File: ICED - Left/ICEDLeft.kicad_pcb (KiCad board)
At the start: 2 copper layers, 175.4 x 145 mm, 164 parts, among them P1 Conn_ARM_JTAG_SWD_10, P2 DX07S024XJ1R1100, P3 CONN_17, P4 692121130100, P5 RGB Out, Q1 TC1264, U1 MK20DX256VLH7, U2 IS31FL3737-QFLS4-TR, X1 CRYSTAL

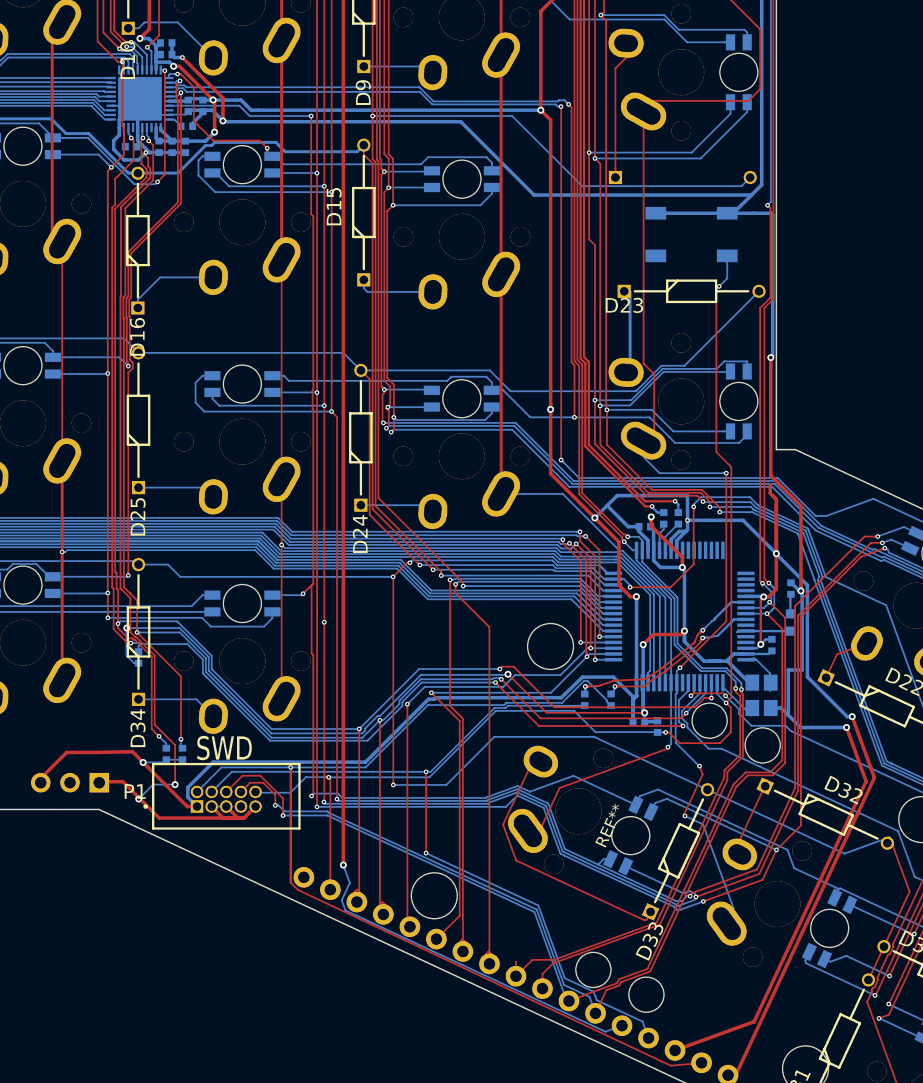
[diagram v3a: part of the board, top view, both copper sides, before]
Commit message: re-added RGBOUT
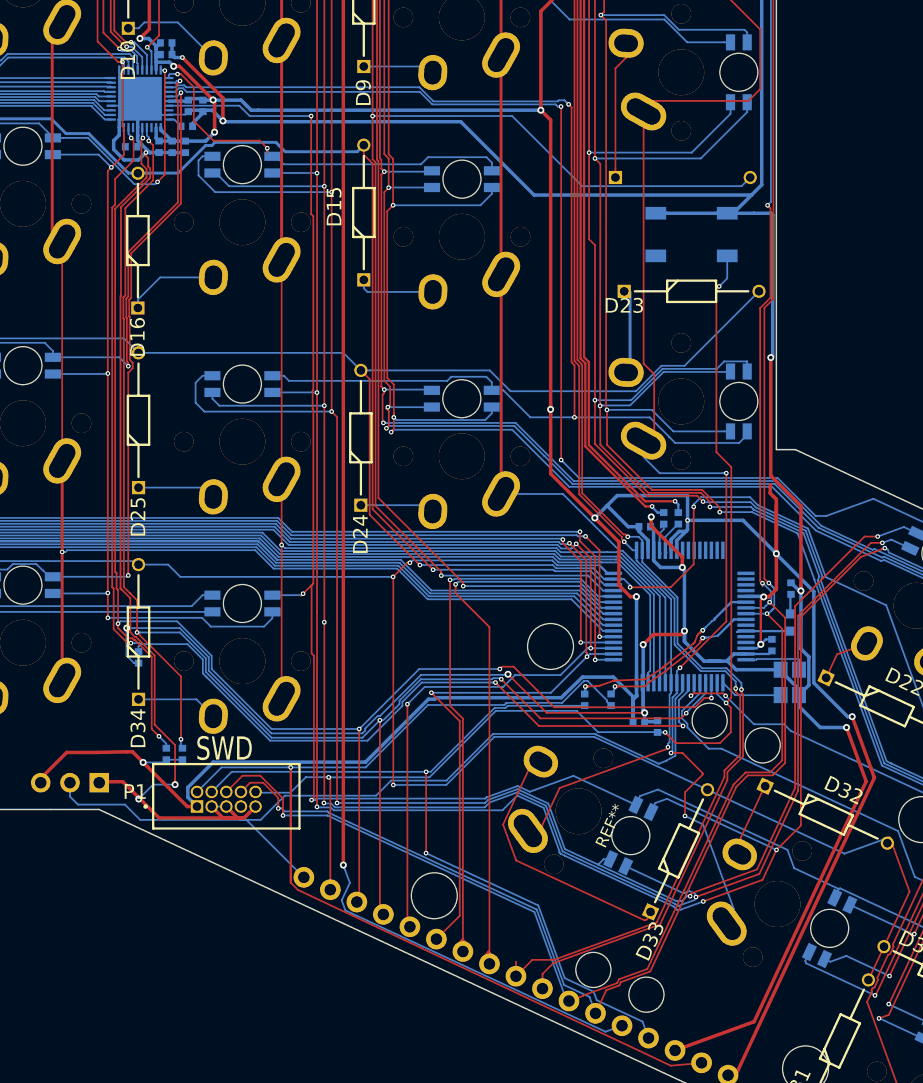
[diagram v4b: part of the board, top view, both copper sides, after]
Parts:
- moved X1 2.70 mm to (147.4, 140.3)
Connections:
- P3 pad 17: (no net) -> /mcu/RGBOUT
- P5 pad 2: (no net) -> /mcu/RGBOUT
- U1 pad 40: (no net) -> /mcu/RGBOUT
- U2 pad 11: (no net) -> VSS
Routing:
- net /mcu/RGBOUT: track 0.00 -> 72.7 mm
- net VSS: track 591.7 -> 596.3 mm
- net Net-(U1-Pad33): track 3.90 -> 5.85 mm
- net /mcu/SCL0: track 135.6 -> 134.0 mm
- net /mcu/SDA0: track 135.6 -> 134.1 mm
- net /Col3: track 118.6 -> 119.9 mm
- net Net-(U1-Pad32): track 4.88 -> 5.56 mm
- net /mcu/ledmatrix_2/Blue1: track 525.5 -> 526.0 mm
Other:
- board text added: "RGBOUT"
- board text removed: "RGBIN"

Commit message: tweaks and cleanup
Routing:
- net /mcu/ledmatrix_2/Blue2: track 455.5 -> 441.8 mm
- net /mcu/ledmatrix_2/Green2: track 435.5 -> 423.5 mm
- net /Col9: track 252.8 -> 241.2 mm
- net /mcu/ledmatrix_2/Green1: track 516.3 -> 509.4 mm, vias 16 -> 15
- net /mcu/ledmatrix_2/Blue1: track 526.0 -> 519.5 mm
- net /mcu/ledmatrix_2/Red1: track 492.5 -> 487.6 mm
- net /mcu/TX1: track 161.3 -> 160.0 mm

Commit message: even more final tweaks
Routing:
- net VDD: track 423.0 -> 413.0 mm
- net /mcu/ledmatrix_2/Blue4: track 152.0 -> 161.0 mm, vias 7 -> 8
- net /mcu/ledmatrix_2/Green4: track 151.3 -> 147.4 mm, vias 8 -> 9
- net /mcu/ledmatrix_2/Row1A: track 107.4 -> 106.4 mm

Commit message: Kailh hotswaps and ground plane
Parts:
- removed STAB1: Stabilizer_Cherry_MX_2u, prettylib:Stabilizer_Cherry_MX_2u
- S1, S10, S11, S12, S13, S14, S15, S16, S17, S18, S19, S2, S20, S21, S22, S23, S24, S25, S26, S27, S28, S29, S3, S30, S31, S32, S33, S34, S35, S36, S37, S38, S4, S5, S6, S7, S8, S9: footprint prettylib:MXALPS -> prettylib:SW_Hotswap_Kailh
- moved R8 6.75 mm to (85.1, 98.1), turned to 0 degrees
- moved C18 6.38 mm to (88.7, 89.1)
- moved U2 6.27 mm to (86.5, 94.0)
- moved C6 6.27 mm to (88.8, 90.2)
- moved C21 6.05 mm to (88.4, 98.0)
- moved R12 5.53 mm to (91.1, 95.8)
- moved D16 5.51 mm to (90.0, 113.2)
- moved C20 5.34 mm to (90.9, 97.3)
- moved C9 5.25 mm to (89.9, 97.3)
- moved C19 4.56 mm to (96.0, 94.8)
- moved C8 4.53 mm to (94.9, 94.7)
- moved C7 4.47 mm to (144.1, 141.1)
- moved D2 4.47 mm to (107.6, 74.4)
- moved LED10 4.47 mm to (98.2, 80.4)
- moved LED23 4.47 mm to (141.3, 120.0)
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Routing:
- net (no net): track 0.00 -> 192.2 mm, vias 0 -> 2
- net /Col3: track 119.9 -> 58.4 mm
- net /Col4: track 109.5 -> 52.5 mm, vias 3 -> 2
- net VSS: track 596.3 -> 541.9 mm, vias 19 -> 20
- net /mcu/ledmatrix_2/Blue1: track 519.5 -> 549.8 mm, vias 15 -> 18
- net VDD: track 413.0 -> 431.6 mm, vias 16 -> 17
- net /mcu/ledmatrix_2/Blue4: track 161.0 -> 172.5 mm, vias 8 -> 9
- net /Col1: track 64.0 -> 74.8 mm
- net /mcu/ledmatrix_2/Row5A: track 115.2 -> 125.6 mm, vias 2 -> 3
- net /mcu/SWD_DIO: track 100.1 -> 90.5 mm
- net /Col6: track 127.7 -> 136.1 mm, vias 1 -> 6
- net /mcu/ledmatrix_2/Blue2: track 441.8 -> 433.5 mm, vias 15 -> 17
- net /mcu/ledmatrix_2/Row3B: track 35.0 -> 42.9 mm
- net Net-(D29-Pad1): track 13.7 -> 21.6 mm
- net /Col9: track 241.2 -> 247.7 mm, vias 1 -> 6
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- added copper zone on B.Cu, net VSS

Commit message: 0606 LEDs
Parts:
- LED1, LED10, LED11, LED12, LED13, LED14, LED15, LED16, LED17, LED18, LED19, LED2, LED20, LED21, LED22, LED23, LED24, LED25, LED26, LED27, LED28, LED29, LED3, LED30, LED31, LED32, LED33, LED34, LED35, LED36, LED37, LED38, LED4, LED5, LED6, LED7, LED8, LED9: value LED_RGBA -> RGB_0606; footprint prettylib:AAA3528SURKCGKC09 -> prettylib:0606
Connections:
- LED1 pad 1: /mcu/ledmatrix_2/Red3 -> /mcu/ledmatrix_2/Row1B
- LED1 pad 2: /mcu/ledmatrix_2/Green3 -> /mcu/ledmatrix_2/Red3
- LED1 pad 3: /mcu/ledmatrix_2/Blue3 -> /mcu/ledmatrix_2/Green3
- LED1 pad 4: /mcu/ledmatrix_2/Row1B -> /mcu/ledmatrix_2/Blue3
- LED10 pad 1: /mcu/ledmatrix_2/Red1 -> /mcu/ledmatrix_2/Row2B
- LED10 pad 2: /mcu/ledmatrix_2/Green1 -> /mcu/ledmatrix_2/Red1
- LED10 pad 3: /mcu/ledmatrix_2/Blue1 -> /mcu/ledmatrix_2/Green1
- LED10 pad 4: /mcu/ledmatrix_2/Row2B -> /mcu/ledmatrix_2/Blue1
- LED11 pad 1: /mcu/ledmatrix_2/Red4 -> /mcu/ledmatrix_2/Row2A
- LED11 pad 2: /mcu/ledmatrix_2/Green4 -> /mcu/ledmatrix_2/Red4
- LED11 pad 3: /mcu/ledmatrix_2/Blue4 -> /mcu/ledmatrix_2/Green4
- LED11 pad 4: /mcu/ledmatrix_2/Row2A -> /mcu/ledmatrix_2/Blue4
- LED12 pad 1: /mcu/ledmatrix_2/Red3 -> /mcu/ledmatrix_2/Row2A
- LED12 pad 2: /mcu/ledmatrix_2/Green3 -> /mcu/ledmatrix_2/Red3
- LED12 pad 3: /mcu/ledmatrix_2/Blue3 -> /mcu/ledmatrix_2/Green3
- LED12 pad 4: /mcu/ledmatrix_2/Row2A -> /mcu/ledmatrix_2/Blue3
- LED13 pad 1: /mcu/ledmatrix_2/Red2 -> /mcu/ledmatrix_2/Row2A
- LED13 pad 2: /mcu/ledmatrix_2/Green2 -> /mcu/ledmatrix_2/Red2
- LED13 pad 3: /mcu/ledmatrix_2/Blue2 -> /mcu/ledmatrix_2/Green2
- LED13 pad 4: /mcu/ledmatrix_2/Row2A -> /mcu/ledmatrix_2/Blue2
- LED14 pad 1: /mcu/ledmatrix_2/Red1 -> /mcu/ledmatrix_2/Row2A
- LED14 pad 2: /mcu/ledmatrix_2/Green1 -> /mcu/ledmatrix_2/Red1
- LED14 pad 3: /mcu/ledmatrix_2/Blue1 -> /mcu/ledmatrix_2/Green1
- LED14 pad 4: /mcu/ledmatrix_2/Row2A -> /mcu/ledmatrix_2/Blue1
- LED15 pad 1: /mcu/ledmatrix_2/Red2 -> /mcu/ledmatrix_2/Row3B
- LED15 pad 2: /mcu/ledmatrix_2/Green2 -> /mcu/ledmatrix_2/Red2
- LED15 pad 3: /mcu/ledmatrix_2/Blue2 -> /mcu/ledmatrix_2/Green2
- LED15 pad 4: /mcu/ledmatrix_2/Row3B -> /mcu/ledmatrix_2/Blue2
- LED16 pad 1: /mcu/ledmatrix_2/Red1 -> /mcu/ledmatrix_2/Row3B
- LED16 pad 2: /mcu/ledmatrix_2/Green1 -> /mcu/ledmatrix_2/Red1
- LED16 pad 3: /mcu/ledmatrix_2/Blue1 -> /mcu/ledmatrix_2/Green1
- LED16 pad 4: /mcu/ledmatrix_2/Row3B -> /mcu/ledmatrix_2/Blue1
- LED17 pad 1: /mcu/ledmatrix_2/Red4 -> /mcu/ledmatrix_2/Row3A
- LED17 pad 2: /mcu/ledmatrix_2/Green4 -> /mcu/ledmatrix_2/Red4
- LED17 pad 3: /mcu/ledmatrix_2/Blue4 -> /mcu/ledmatrix_2/Green4
- LED17 pad 4: /mcu/ledmatrix_2/Row3A -> /mcu/ledmatrix_2/Blue4
- LED18 pad 1: /mcu/ledmatrix_2/Red3 -> /mcu/ledmatrix_2/Row3A
- LED18 pad 2: /mcu/ledmatrix_2/Green3 -> /mcu/ledmatrix_2/Red3
- LED18 pad 3: /mcu/ledmatrix_2/Blue3 -> /mcu/ledmatrix_2/Green3
- LED18 pad 4: /mcu/ledmatrix_2/Row3A -> /mcu/ledmatrix_2/Blue3
- LED19 pad 1: /mcu/ledmatrix_2/Red2 -> /mcu/ledmatrix_2/Row3A
- LED19 pad 2: /mcu/ledmatrix_2/Green2 -> /mcu/ledmatrix_2/Red2
- LED19 pad 3: /mcu/ledmatrix_2/Blue2 -> /mcu/ledmatrix_2/Green2
- LED19 pad 4: /mcu/ledmatrix_2/Row3A -> /mcu/ledmatrix_2/Blue2
- LED2 pad 1: /mcu/ledmatrix_2/Red2 -> /mcu/ledmatrix_2/Row1B
- LED2 pad 2: /mcu/ledmatrix_2/Green2 -> /mcu/ledmatrix_2/Red2
- LED2 pad 3: /mcu/ledmatrix_2/Blue2 -> /mcu/ledmatrix_2/Green2
- LED2 pad 4: /mcu/ledmatrix_2/Row1B -> /mcu/ledmatrix_2/Blue2
- LED20 pad 1: /mcu/ledmatrix_2/Red1 -> /mcu/ledmatrix_2/Row3A
- LED20 pad 2: /mcu/ledmatrix_2/Green1 -> /mcu/ledmatrix_2/Red1
- LED20 pad 3: /mcu/ledmatrix_2/Blue1 -> /mcu/ledmatrix_2/Green1
- LED20 pad 4: /mcu/ledmatrix_2/Row3A -> /mcu/ledmatrix_2/Blue1
- LED21 pad 1: /mcu/ledmatrix_2/Red2 -> /mcu/ledmatrix_2/Row4C
- LED21 pad 2: /mcu/ledmatrix_2/Green2 -> /mcu/ledmatrix_2/Red2
- LED21 pad 3: /mcu/ledmatrix_2/Blue2 -> /mcu/ledmatrix_2/Green2
- LED21 pad 4: /mcu/ledmatrix_2/Row4C -> /mcu/ledmatrix_2/Blue2
- LED22 pad 1: /mcu/ledmatrix_2/Red1 -> /mcu/ledmatrix_2/Row4C
- LED22 pad 2: /mcu/ledmatrix_2/Green1 -> /mcu/ledmatrix_2/Red1
- LED22 pad 3: /mcu/ledmatrix_2/Blue1 -> /mcu/ledmatrix_2/Green1
- LED22 pad 4: /mcu/ledmatrix_2/Row4C -> /mcu/ledmatrix_2/Blue1
- LED23 pad 1: /mcu/ledmatrix_2/Red3 -> /mcu/ledmatrix_2/Row4B
- LED23 pad 2: /mcu/ledmatrix_2/Green3 -> /mcu/ledmatrix_2/Red3
- LED23 pad 3: /mcu/ledmatrix_2/Blue3 -> /mcu/ledmatrix_2/Green3
- LED23 pad 4: /mcu/ledmatrix_2/Row4B -> /mcu/ledmatrix_2/Blue3
- LED24 pad 1: /mcu/ledmatrix_2/Red2 -> /mcu/ledmatrix_2/Row4B
- LED24 pad 2: /mcu/ledmatrix_2/Green2 -> /mcu/ledmatrix_2/Red2
- LED24 pad 3: /mcu/ledmatrix_2/Blue2 -> /mcu/ledmatrix_2/Green2
- LED24 pad 4: /mcu/ledmatrix_2/Row4B -> /mcu/ledmatrix_2/Blue2
- LED25 pad 1: /mcu/ledmatrix_2/Red1 -> /mcu/ledmatrix_2/Row4B
- LED25 pad 2: /mcu/ledmatrix_2/Green1 -> /mcu/ledmatrix_2/Red1
- LED25 pad 3: /mcu/ledmatrix_2/Blue1 -> /mcu/ledmatrix_2/Green1
- LED25 pad 4: /mcu/ledmatrix_2/Row4B -> /mcu/ledmatrix_2/Blue1
- LED26 pad 1: /mcu/ledmatrix_2/Red4 -> /mcu/ledmatrix_2/Row4A
- LED26 pad 2: /mcu/ledmatrix_2/Green4 -> /mcu/ledmatrix_2/Red4
- LED26 pad 3: /mcu/ledmatrix_2/Blue4 -> /mcu/ledmatrix_2/Green4
- LED26 pad 4: /mcu/ledmatrix_2/Row4A -> /mcu/ledmatrix_2/Blue4
- LED27 pad 1: /mcu/ledmatrix_2/Red3 -> /mcu/ledmatrix_2/Row4A
- LED27 pad 2: /mcu/ledmatrix_2/Green3 -> /mcu/ledmatrix_2/Red3
- LED27 pad 3: /mcu/ledmatrix_2/Blue3 -> /mcu/ledmatrix_2/Green3
- LED27 pad 4: /mcu/ledmatrix_2/Row4A -> /mcu/ledmatrix_2/Blue3
- LED28 pad 1: /mcu/ledmatrix_2/Red2 -> /mcu/ledmatrix_2/Row4A
- LED28 pad 2: /mcu/ledmatrix_2/Green2 -> /mcu/ledmatrix_2/Red2
- LED28 pad 3: /mcu/ledmatrix_2/Blue2 -> /mcu/ledmatrix_2/Green2
- LED28 pad 4: /mcu/ledmatrix_2/Row4A -> /mcu/ledmatrix_2/Blue2
- LED29 pad 1: /mcu/ledmatrix_2/Red1 -> /mcu/ledmatrix_2/Row4A
- LED29 pad 2: /mcu/ledmatrix_2/Green1 -> /mcu/ledmatrix_2/Red1
- LED29 pad 3: /mcu/ledmatrix_2/Blue1 -> /mcu/ledmatrix_2/Green1
- LED29 pad 4: /mcu/ledmatrix_2/Row4A -> /mcu/ledmatrix_2/Blue1
- LED3 pad 1: /mcu/ledmatrix_2/Red1 -> /mcu/ledmatrix_2/Row1B
- LED3 pad 2: /mcu/ledmatrix_2/Green1 -> /mcu/ledmatrix_2/Red1
- LED3 pad 3: /mcu/ledmatrix_2/Blue1 -> /mcu/ledmatrix_2/Green1
- LED3 pad 4: /mcu/ledmatrix_2/Row1B -> /mcu/ledmatrix_2/Blue1
- LED30 pad 1: /mcu/ledmatrix_2/Red3 -> /mcu/ledmatrix_2/Row4C
- LED30 pad 2: /mcu/ledmatrix_2/Green3 -> /mcu/ledmatrix_2/Red3
- LED30 pad 3: /mcu/ledmatrix_2/Blue3 -> /mcu/ledmatrix_2/Green3
- LED30 pad 4: /mcu/ledmatrix_2/Row4C -> /mcu/ledmatrix_2/Blue3
- LED31 pad 1: /mcu/ledmatrix_2/Red3 -> /mcu/ledmatrix_2/Row5B
- LED31 pad 2: /mcu/ledmatrix_2/Green3 -> /mcu/ledmatrix_2/Red3
- LED31 pad 3: /mcu/ledmatrix_2/Blue3 -> /mcu/ledmatrix_2/Green3
- LED31 pad 4: /mcu/ledmatrix_2/Row5B -> /mcu/ledmatrix_2/Blue3
- LED32 pad 1: /mcu/ledmatrix_2/Red2 -> /mcu/ledmatrix_2/Row5B
- LED32 pad 2: /mcu/ledmatrix_2/Green2 -> /mcu/ledmatrix_2/Red2
- LED32 pad 3: /mcu/ledmatrix_2/Blue2 -> /mcu/ledmatrix_2/Green2
- LED32 pad 4: /mcu/ledmatrix_2/Row5B -> /mcu/ledmatrix_2/Blue2
- LED33 pad 1: /mcu/ledmatrix_2/Red1 -> /mcu/ledmatrix_2/Row5B
- LED33 pad 2: /mcu/ledmatrix_2/Green1 -> /mcu/ledmatrix_2/Red1
- LED33 pad 3: /mcu/ledmatrix_2/Blue1 -> /mcu/ledmatrix_2/Green1
- LED33 pad 4: /mcu/ledmatrix_2/Row5B -> /mcu/ledmatrix_2/Blue1
- LED34 pad 1: /mcu/ledmatrix_2/Red4 -> /mcu/ledmatrix_2/Row5B
- LED34 pad 2: /mcu/ledmatrix_2/Green4 -> /mcu/ledmatrix_2/Red4
- LED34 pad 3: /mcu/ledmatrix_2/Blue4 -> /mcu/ledmatrix_2/Green4
- LED34 pad 4: /mcu/ledmatrix_2/Row5B -> /mcu/ledmatrix_2/Blue4
- LED35 pad 1: /mcu/ledmatrix_2/Red4 -> /mcu/ledmatrix_2/Row5A
- LED35 pad 2: /mcu/ledmatrix_2/Green4 -> /mcu/ledmatrix_2/Red4
- LED35 pad 3: /mcu/ledmatrix_2/Blue4 -> /mcu/ledmatrix_2/Green4
- LED35 pad 4: /mcu/ledmatrix_2/Row5A -> /mcu/ledmatrix_2/Blue4
- LED36 pad 1: /mcu/ledmatrix_2/Red3 -> /mcu/ledmatrix_2/Row5A
- LED36 pad 2: /mcu/ledmatrix_2/Green3 -> /mcu/ledmatrix_2/Red3
- LED36 pad 3: /mcu/ledmatrix_2/Blue3 -> /mcu/ledmatrix_2/Green3
- LED36 pad 4: /mcu/ledmatrix_2/Row5A -> /mcu/ledmatrix_2/Blue3
- LED37 pad 1: /mcu/ledmatrix_2/Red2 -> /mcu/ledmatrix_2/Row5A
- LED37 pad 2: /mcu/ledmatrix_2/Green2 -> /mcu/ledmatrix_2/Red2
- LED37 pad 3: /mcu/ledmatrix_2/Blue2 -> /mcu/ledmatrix_2/Green2
- LED37 pad 4: /mcu/ledmatrix_2/Row5A -> /mcu/ledmatrix_2/Blue2
- LED38 pad 1: /mcu/ledmatrix_2/Red1 -> /mcu/ledmatrix_2/Row5A
- LED38 pad 2: /mcu/ledmatrix_2/Green1 -> /mcu/ledmatrix_2/Red1
- LED38 pad 3: /mcu/ledmatrix_2/Blue1 -> /mcu/ledmatrix_2/Green1
- LED38 pad 4: /mcu/ledmatrix_2/Row5A -> /mcu/ledmatrix_2/Blue1
- LED4 pad 1: /mcu/ledmatrix_2/Red4 -> /mcu/ledmatrix_2/Row1A
- LED4 pad 2: /mcu/ledmatrix_2/Green4 -> /mcu/ledmatrix_2/Red4
- LED4 pad 3: /mcu/ledmatrix_2/Blue4 -> /mcu/ledmatrix_2/Green4
- LED4 pad 4: /mcu/ledmatrix_2/Row1A -> /mcu/ledmatrix_2/Blue4
- LED5 pad 1: /mcu/ledmatrix_2/Red3 -> /mcu/ledmatrix_2/Row1A
- LED5 pad 2: /mcu/ledmatrix_2/Green3 -> /mcu/ledmatrix_2/Red3
- LED5 pad 3: /mcu/ledmatrix_2/Blue3 -> /mcu/ledmatrix_2/Green3
- LED5 pad 4: /mcu/ledmatrix_2/Row1A -> /mcu/ledmatrix_2/Blue3
- LED6 pad 1: /mcu/ledmatrix_2/Red2 -> /mcu/ledmatrix_2/Row1A
- LED6 pad 2: /mcu/ledmatrix_2/Green2 -> /mcu/ledmatrix_2/Red2
- LED6 pad 3: /mcu/ledmatrix_2/Blue2 -> /mcu/ledmatrix_2/Green2
- LED6 pad 4: /mcu/ledmatrix_2/Row1A -> /mcu/ledmatrix_2/Blue2
- LED7 pad 1: /mcu/ledmatrix_2/Red1 -> /mcu/ledmatrix_2/Row1A
- LED7 pad 2: /mcu/ledmatrix_2/Green1 -> /mcu/ledmatrix_2/Red1
- LED7 pad 3: /mcu/ledmatrix_2/Blue1 -> /mcu/ledmatrix_2/Green1
- LED7 pad 4: /mcu/ledmatrix_2/Row1A -> /mcu/ledmatrix_2/Blue1
- LED8 pad 1: /mcu/ledmatrix_2/Red3 -> /mcu/ledmatrix_2/Row2B
- LED8 pad 2: /mcu/ledmatrix_2/Green3 -> /mcu/ledmatrix_2/Red3
- LED8 pad 3: /mcu/ledmatrix_2/Blue3 -> /mcu/ledmatrix_2/Green3
- LED8 pad 4: /mcu/ledmatrix_2/Row2B -> /mcu/ledmatrix_2/Blue3
- LED9 pad 1: /mcu/ledmatrix_2/Red2 -> /mcu/ledmatrix_2/Row2B
- LED9 pad 2: /mcu/ledmatrix_2/Green2 -> /mcu/ledmatrix_2/Red2
- LED9 pad 3: /mcu/ledmatrix_2/Blue2 -> /mcu/ledmatrix_2/Green2
- LED9 pad 4: /mcu/ledmatrix_2/Row2B -> /mcu/ledmatrix_2/Blue2
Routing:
- net (no net): track 192.2 -> 191.2 mm
